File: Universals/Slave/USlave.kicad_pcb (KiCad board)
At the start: 2 copper layers, 87.8 x 71.9 mm, 31 parts, among them J1 Power In, J2 I2C Test Point, J3 ISCP, J4 I2C Through, J5 I2C In, J6 0-3, J7 4-7, J8 8-11, J9 12-15, SW1 Reset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

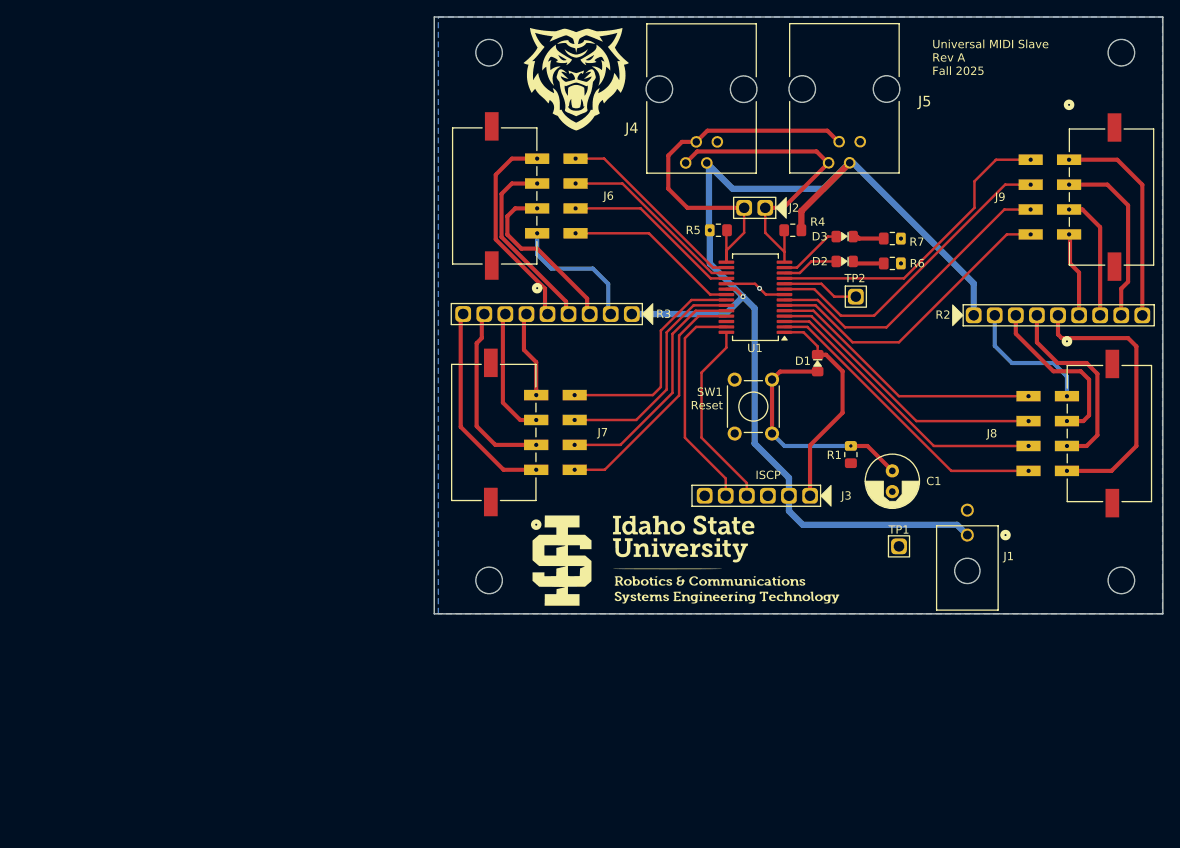
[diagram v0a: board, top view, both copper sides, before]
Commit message: made pdfs for final report
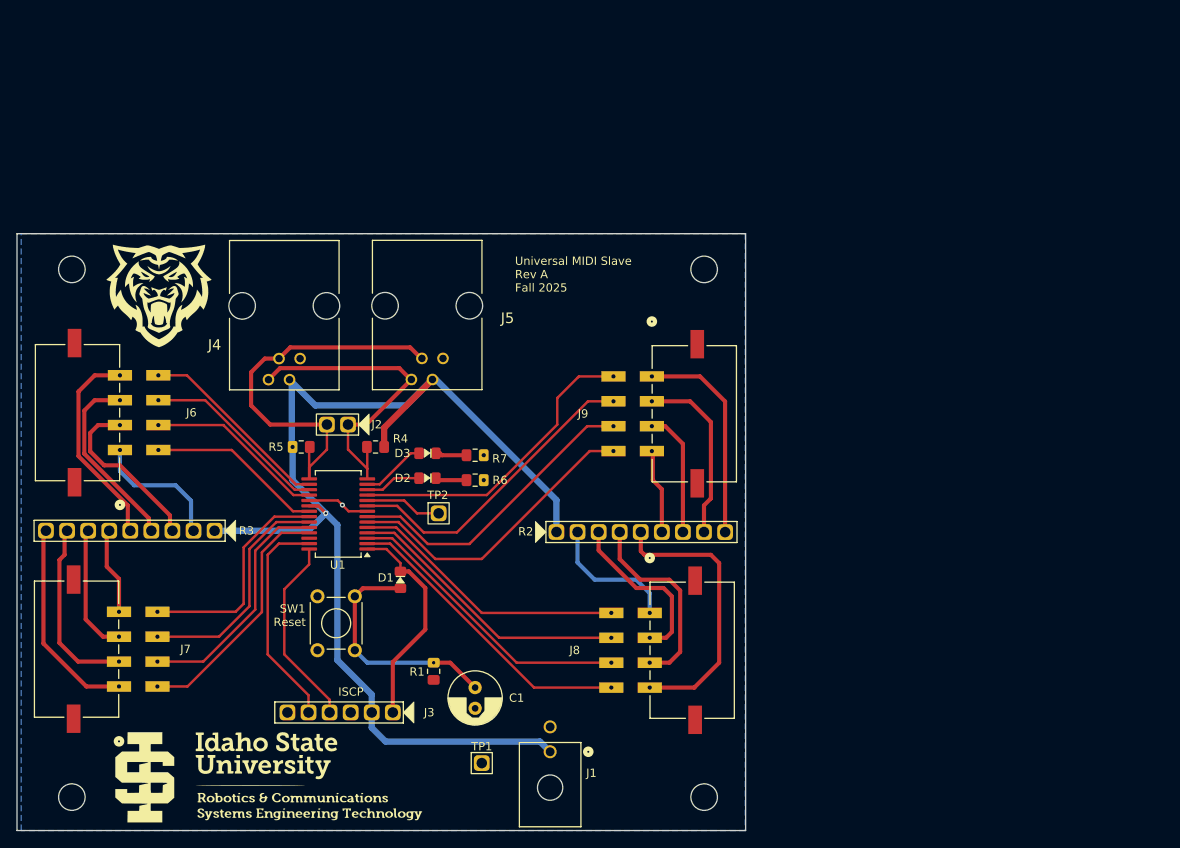
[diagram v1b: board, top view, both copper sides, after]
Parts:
- moved J2 56.7 mm to (115.1, 92.4)
- moved C1 56.7 mm to (150.7, 124.1)
- moved D1 56.7 mm to (141.0, 111.4)
- moved D2 56.7 mm to (144.7, 98.1)
- moved D3 56.7 mm to (144.7, 95.1)
- moved G*** 56.7 mm to (112.6, 76.9)
- moved J1 56.7 mm to (159.8, 131.9)
- moved J4 56.7 mm to (127.7, 78.1)
- moved J6 56.7 mm to (102.8, 91.0)
- moved J7 56.7 mm to (102.7, 119.5)
- moved J8 56.7 mm to (176.9, 119.6)
- moved J9 56.7 mm to (177.1, 91.1)
- moved R1 56.7 mm to (145.7, 122.2)
- moved R2 56.7 mm to (169.4, 103.8)
- moved R3 56.7 mm to (110.5, 106.8)
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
